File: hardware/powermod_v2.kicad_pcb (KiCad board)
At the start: 4 copper layers, 65 x 30 mm, 75 parts, among them J1 USB_C_IN, J2 USB_C_OUT, J3 JST_PH_2, J4 STEMMA_QT, J5 UPDI_HDR, Q1 AON7407, Q2 AON7407, Q3 BSS138, SW1 BUTTON, U1 BM8563, U2 ATtiny1617, U3 TPS63020DSJR, U4 TP4056, U5 XC6206P332MR, Y1 32.768kHz

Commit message: hardware: full electrical verification pass + R28 (CE pull-up) + ADC ref
Reconfirmed the schematic against fresh datasheet evidence, not recall
(user-requested gate before continuing v1/v2 layout work):

- TPS63020: pin-function table extracted from TI's PDF -- all 14 pins +
  EP=PGND match netlist.py exactly. VFB=500mV; our JP2-closed divider is
  TI's own 3.3V table row (1M/180k); open computes 5.00V. Switch limit
  4A typ confirmed; C16 satisfies the VINA bypass rule (<=0.22uF).
- AON7407: package confirmed DFN3x3-8 EP=D (footprint correct); gate
  drives checked against the +/-8V VGS limit: Q1 -3.57V driven, Q2 worst
  +/-5.25V, all safe and past the -3.0V/25mOhm requirement point.
- OR stage walked end-to-end: body-diode orientations, default states in
  MCU reset, soft-start (C12+R11), VBUS bleed, clean charge termination
  (Q2 hard-off on mains means the charger never sees load current).
- BM8563/diode-OR: D3/D4 cathodes on RTC_VDD verified in source (netlist
  golden vectors cover them); 3.3V bus vs diode-dropped RTC_VDD is legal
  (PCF8563-class inputs rated to 6.5V independent of VDD).
- ERC 0 violations, netlist self-test passes: 72 components, 236 pins.

Two findings, both closed here:

1. R28 100k CHG_CE -> VBUS (new). Without it TP4056's CE floats whenever
   PC4 is high-Z (MCU reset, UPDI, unprogrammed) -- undefined charger
   state. Pull-UP so a dead-MCU board still charges (charging-autonomy
   policy); PC4 push-pull overrides. Placed in v2 (courtyards still 0
   overlaps, pads bind VBUS/CHG_CE). The frozen v1 board predates it --
   noted in the doc; v1 was already marked not-fab-ready.

2. ADC reference constraint documented: the spec deferred "re-check
   divider ratio vs chosen reference at schematic time" and it never
   landed. With 1M/330k, VBUS@5.25V presents 1.30V -- the 1.1V internal
   ref CLIPS. Firmware must use the 1.5V internal reference (both
   channels then fit; VBAT max 1.04V). Now in powermod-schematic.md as
   a hardware-imposed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
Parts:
- added R28: 100k, R_0402_1005Metric, F.Cu at (20.1, 11.5)

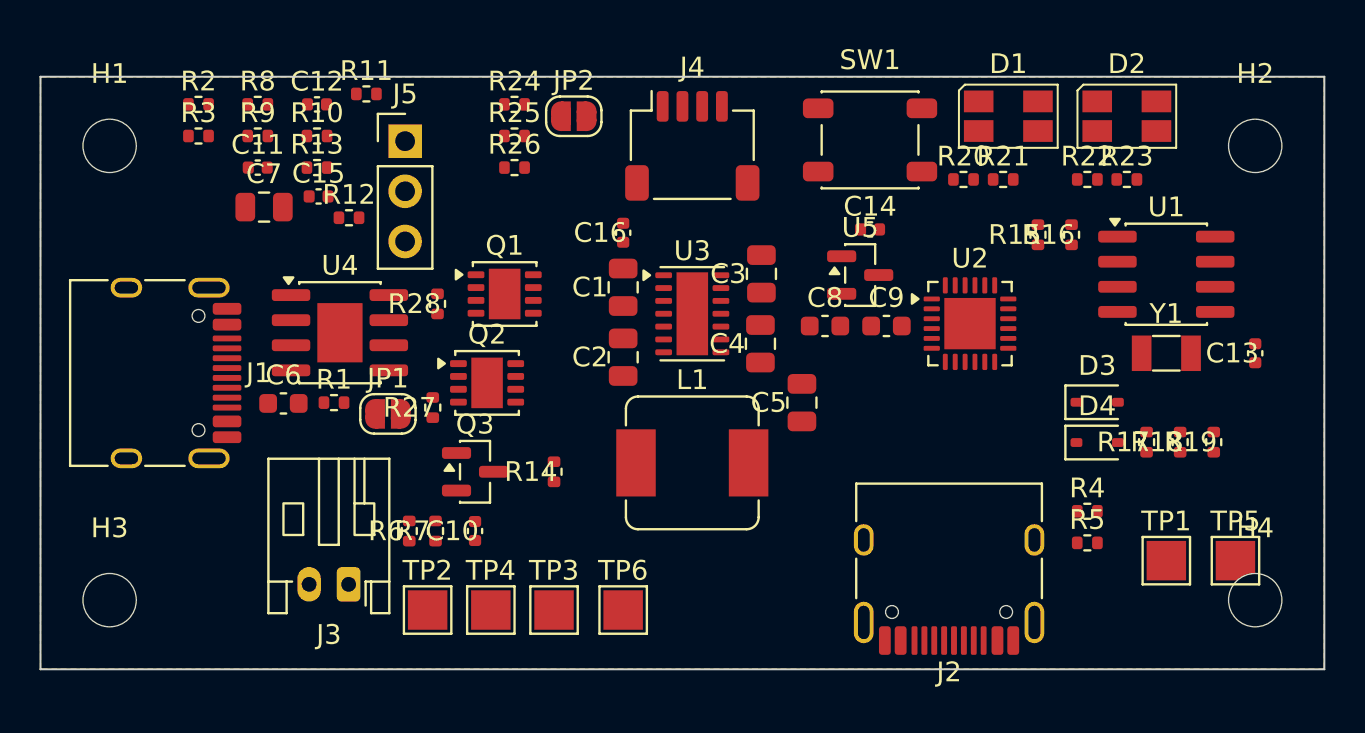
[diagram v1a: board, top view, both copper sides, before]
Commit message: hardware: v2 placement fixes (J2/LEDs) + cleaner no-pours routing (~92%)
Placement corrections from visual review:
- J2 (USB-C out) was rotated 180 -> opening faced INTO the board; a plug
  could not be inserted. Now rot 0, facing out the south edge, like J1
  faces out the west edge. Orientation model confirmed against J1.
- D1/D2 LEDs aligned at the same height, evenly spaced, each with its two
  current-limit resistors grouped directly below (were stranded 15mm away
  by the RTC). J5 (UPDI, location-flexible) moved to the south band to
  make room. 0 courtyard overlaps, verified against KiCad.

Routing approach changed: dropped the F.Cu power pad-field pours (gated
behind PADPOURS=1). They absorbed the USB-C escapes but FRAGMENT around
foreign pads, and each fragment then needs stitching -- which my batch
finisher did unsafely (introduced 2 shorts + 6 dangling vias by trusting
geometry without per-trial DRC). Plain enforced-width traces are cleaner:
Freerouting escapes the 0.5mm-pitch USB-C pads fine at the 0.3mm class
minimum, and there are no fragments to chase.

Result: ~92% routed, and importantly CLEAN -- 0 shorts, 0 dangling, 0
footprint errors. Freerouting completes all but ~6 last-mile nets (VOUT,
VBUS, 3V3, SDA); GND fully stitched to the In1 plane (grid + geometry-
verified fragment fill). Error-severity DRC: 9 unconnected + 5 track_width
(power escapes marginally under min); the ~150 remaining all-severity
items are silkscreen-cosmetic.

The last 6 nets are the classic autorouter tail on a dense fine-pitch
board -- they close with a topological router (TopoR, DSN handoff ready
in powermod_v2_for_topor.dsn) or ~30 min interactive in KiCad, not more
batch scripting. finish_v2.py kept as a fast batch finisher but removed
from the pipeline (unsafe without per-trial validation).

Co-Authored-By: Claude Opus 4.8 <noreply@anthropic.com>
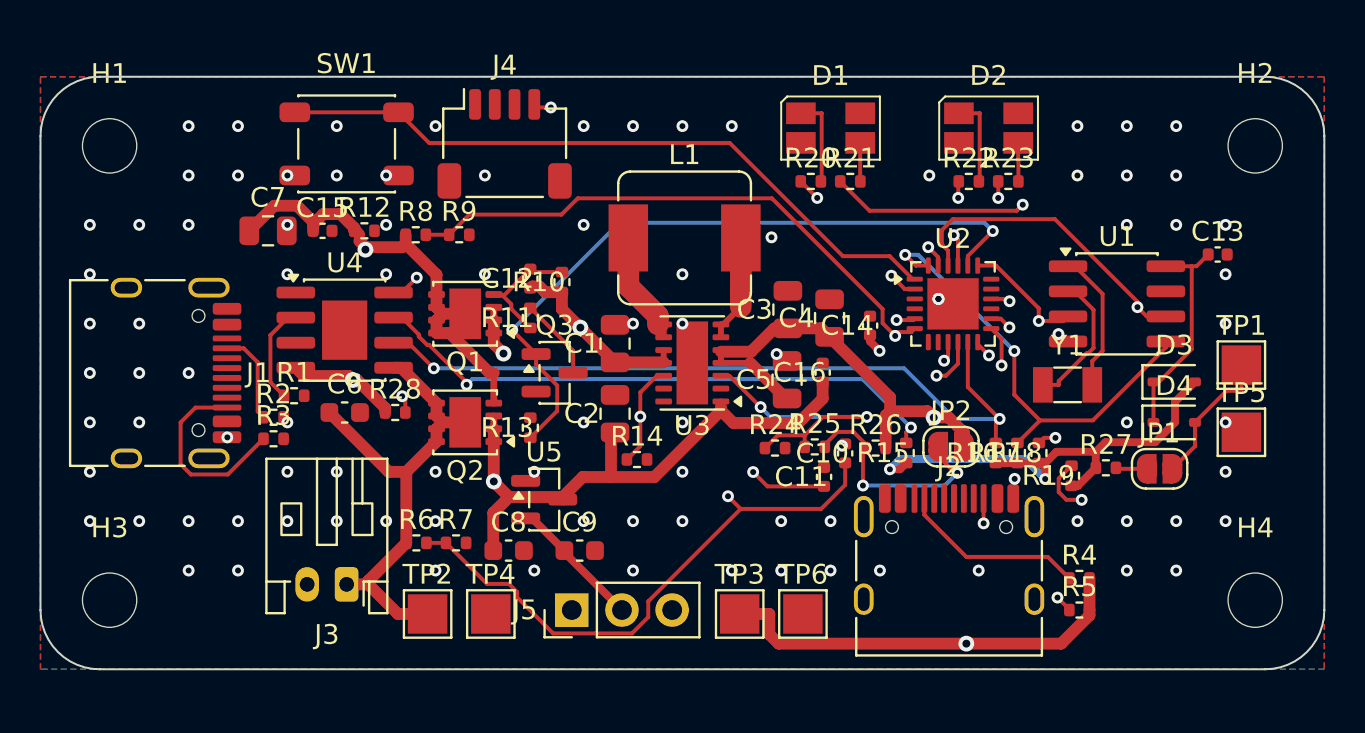
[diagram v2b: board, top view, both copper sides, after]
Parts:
- moved JP1 39.2 mm to (56.7, 19.9)
- moved R27 34.2 mm to (53.9, 19.8), turned to 0 degrees
- moved C11 32.7 mm to (39.7, 20.3), turned to 90 degrees
- moved SW1 26.5 mm to (15.5, 3.40)
- moved JP2 25.4 mm to (46.1, 18.7)
- moved J5 25.2 mm to (26.9, 27.0), turned to 90 degrees
- moved R26 23.1 mm to (42.3, 18.8)
- moved R25 21.9 mm to (39.2, 18.7)
- moved R24 21.8 mm to (37.2, 18.8)
- moved C8 19.6 mm to (23.7, 24.0)
- moved U5 19.6 mm to (25.5, 21.4)
- moved C9 19.2 mm to (27.3, 24.0)
- moved C10 19.1 mm to (40.7, 19.1)
- moved R13 17.0 mm to (24.8, 17.8), turned to 90 degrees
- moved R2 16.3 mm to (11.8, 17.2)
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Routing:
- net VOUT: track 0.00 -> 56.3 mm, vias 0 -> 2
- net 3V3: track 0.00 -> 55.5 mm, vias 0 -> 3
- net VSYS: track 0.00 -> 52.9 mm, vias 0 -> 3
- net VBUS_DIV: track 0.00 -> 43.4 mm, vias 0 -> 2
- net VBAT_DIV: track 0.00 -> 42.7 mm, vias 0 -> 2
- net CHG_CE: track 0.00 -> 40.5 mm, vias 0 -> 3
- net CHG_STDBY: track 0.00 -> 38.1 mm, vias 0 -> 2
- net CHG_CHRG: track 0.00 -> 36.3 mm, vias 0 -> 3
- net Q1_GATE_DRV: track 0.00 -> 36.0 mm, vias 0 -> 2
- net VBUS: track 0.00 -> 35.3 mm, vias 0 -> 2
- net BUTTON: track 0.00 -> 34.9 mm
- net SCL: track 0.00 -> 32.5 mm, vias 0 -> 2
- net UPDI: track 0.00 -> 27.7 mm, vias 0 -> 1
- net RTC_SCL: track 0.00 -> 25.0 mm, vias 0 -> 2
- net VBAT: track 0.00 -> 24.8 mm
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- removed copper zone on In2.Cu, net VBUS
- removed copper zone on In2.Cu, net VOUT
- removed copper zone on In2.Cu, net VSYS
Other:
- outline, holes or cut-outs redrawn
